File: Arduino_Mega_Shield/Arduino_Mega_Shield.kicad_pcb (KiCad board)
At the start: 4 copper layers, 99.5 x 53.3 mm, 58 parts, among them J1 Conn_01x04, J10 SW10, J11 SW6, J12 SW7, J13 SW8, J14 SW9, J15 Motor Driver Connector, J16 Motor Driver Connector, J17 Motor Driver Connector, J18 Motor Driver Connector, J19 Screw_Terminal_01x02, J2 Conn_01x04, J20 JOYSTICK, J21 I2C CONNECTOR, J22 ENCODER1, J23 ENCODER2, J24 ENCODER3, J25 ENCODER4, J26 UART CONNECTOR, J27 3_pin_selector, J28 3_pin_selector, J29 3_pin_selector, J3 Conn_01x04, J30 3_pin_selector, J31 3_pin_selector, J32 3_pin_selector, J33 3_pin_selector, J34 3_pin_selector, J35 3_pin_selector, J36 3_pin_selector, J37 3_pin_selector, J38 3_pin_selector, J4 Conn_01x04, J5 SW5, J6 SW1, J7 SW2, J8 SW3, J9 SW4

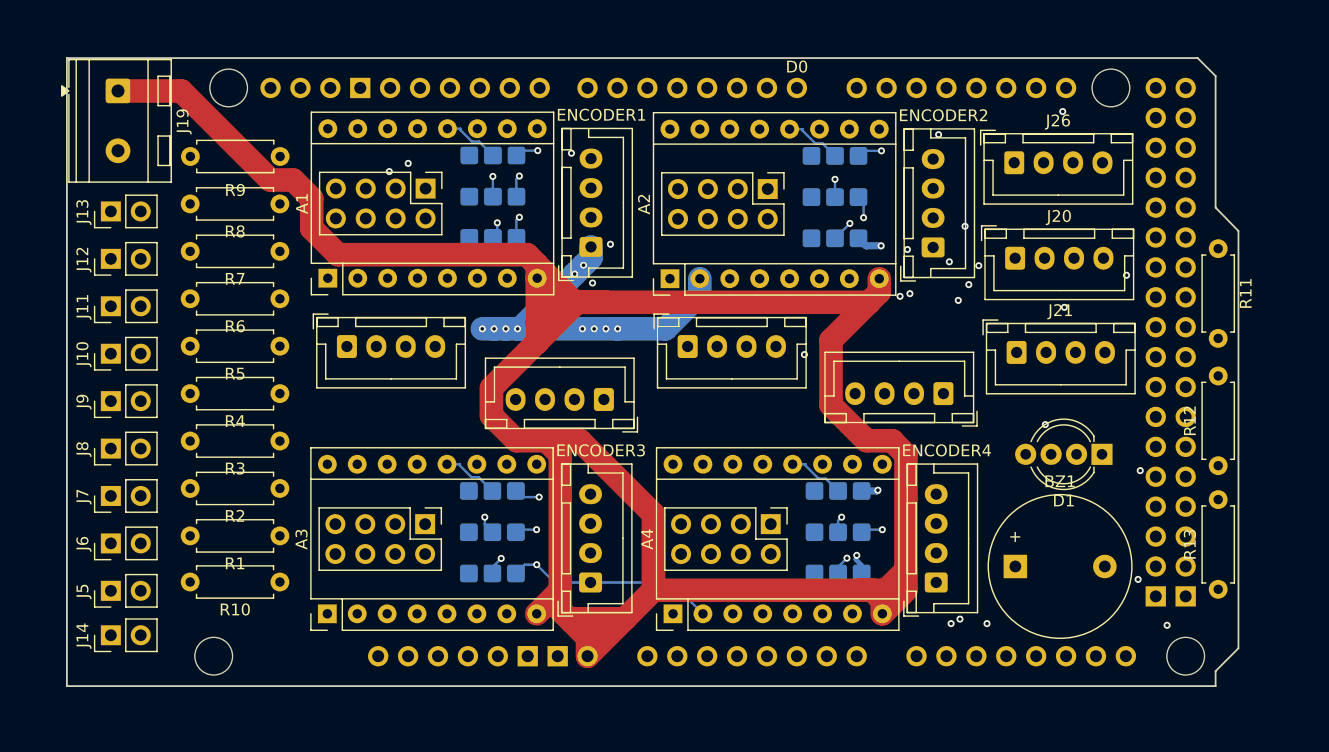
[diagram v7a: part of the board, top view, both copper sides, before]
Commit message: Avancement on the silkscreen of the PCB
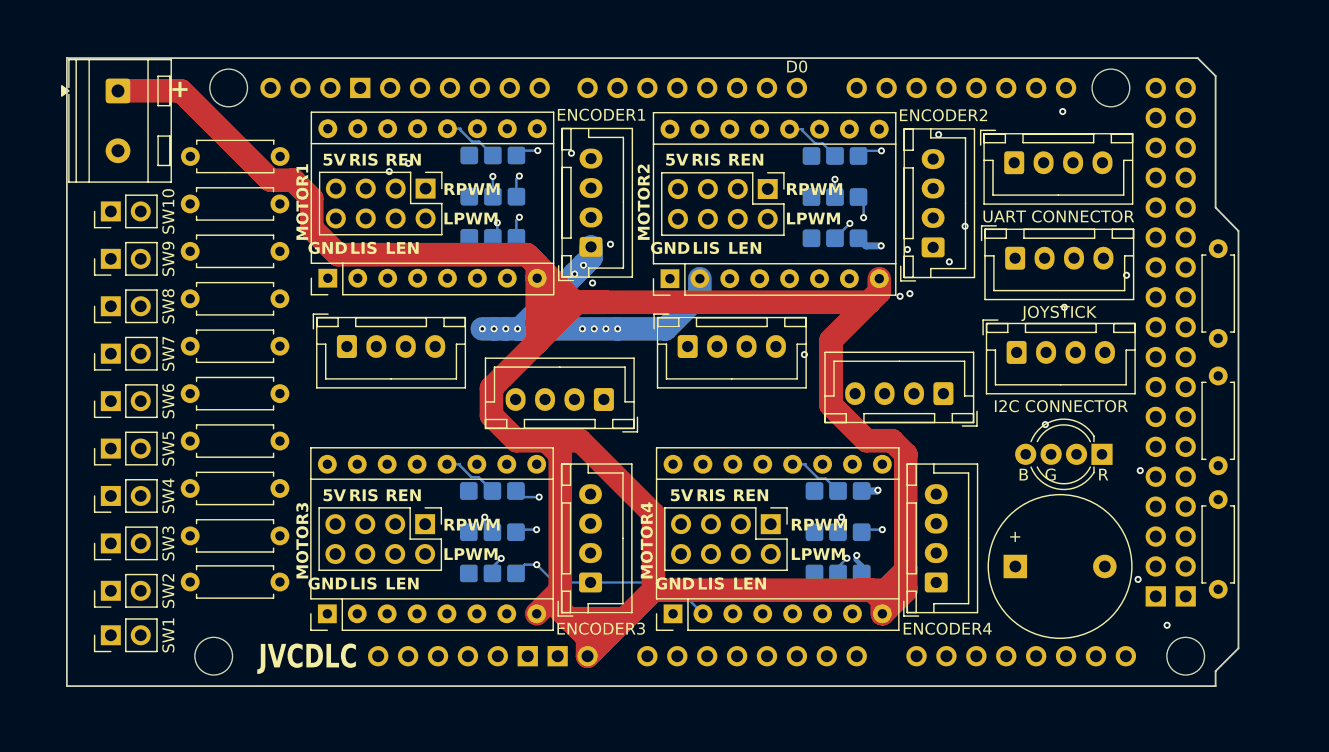
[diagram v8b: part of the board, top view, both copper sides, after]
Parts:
- J11: renamed from J9; value SW4 -> SW6
- J12: renamed from J10; value SW10 -> SW7
- J13: renamed from J11; value SW6 -> SW8
- J14: renamed from J12; value SW7 -> SW9
- J39: renamed from J13; value SW8 -> SW10
- J5: renamed from J8; value SW3 -> SW5
- J6: renamed from J14; value SW9 -> SW1
- J7: renamed from J5; value SW5 -> SW2
- J8: renamed from J6; value SW1 -> SW3
- J9: renamed from J7; value SW2 -> SW4
- renumbered R4 to R1, R8 to R10, R10 to R2, R1 to R3, R2 to R4, R3 to R5, R9 to R6, R5 to R7, R6 to R8, R7 to R9
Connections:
- J11 pad 2: SW4 -> SW6
- J12 pad 2: SW10 -> SW7
- J13 pad 2: SW6 -> SW8
- J14 pad 2: SW7 -> SW9
- J39 pad 2: SW8 -> SW10
- J5 pad 2: SW3 -> SW5
- J6 pad 2: SW9 -> SW1
- J7 pad 2: SW5 -> SW2
- J8 pad 2: SW1 -> SW3
- J9 pad 2: SW2 -> SW4
- R1 pad 2: SW3 -> SW5
- R10 pad 2: SW7 -> SW9
- R2 pad 2: SW9 -> SW1
- R3 pad 2: SW5 -> SW2
- R4 pad 2: SW1 -> SW3
- R5 pad 2: SW2 -> SW4
- R6 pad 2: SW8 -> SW10
- R7 pad 2: SW4 -> SW6
- R8 pad 2: SW10 -> SW7
- R9 pad 2: SW6 -> SW8
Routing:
- net SW8: track 123.5 -> 0.00 mm, vias 1 -> 0
- net SW7: track 114.1 -> 0.00 mm, vias 1 -> 0
- net SW6: track 109.6 -> 0.00 mm, vias 1 -> 0
- net SW4: track 90.0 -> 0.00 mm, vias 1 -> 0
- net SW5: track 86.5 -> 0.00 mm
- net SW3: track 86.1 -> 0.00 mm, vias 1 -> 0
- net SW2: track 83.2 -> 0.00 mm, vias 1 -> 0
- net SW1: track 77.6 -> 0.00 mm
- net SW9: track 57.0 -> 0.00 mm
- net SW10: track 35.5 -> 0.00 mm
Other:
- board text added: "+"
- board text added: "5V"
- board text added: "B"
- board text added: "B2 A2 A1 B1"
- board text added: "DIR"
- board text added: "EN"
- board text added: "ENC_A"
- board text added: "ENC_B"
- board text added: "G"
- board text added: "GND"
- board text added: "JVCDLC"
- board text added: "LEN"
- board text added: "LIS"
- board text added: "LPWM"
- board text added: "MOTOR1"
- board text added: "MOTOR2"
- board text added: "MOTOR3"
- board text added: "MOTOR4"
- board text added: "Made by Josserand-Pierre Gay with the help of Simon Guillemette"
- board text added: "R"
- board text added: "REN"
- board text added: "RESET"
- board text added: "RIS"
- board text added: "RPWM"
- board text added: "RX2"
- board text added: "SCL"
- board text added: "SDA"
- board text added: "SLEEP"
- board text added: "STEP"
- board text added: "TX2"
- board text added: "VRX"
- board text added: "VRY"
